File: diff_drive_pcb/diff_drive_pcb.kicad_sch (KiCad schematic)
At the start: 13 parts, among them J1 Conn_01x02_Pin, J10 Conn_01x02_Pin, J2 Conn_01x04_Socket, J3 Conn_01x02_Pin, J4 Conn_01x04_Socket, J5 Conn_01x02_Pin, J6 Conn_01x04_Socket, J7 Conn_01x02_Pin, J8 Conn_01x04_Socket, J9 Conn_01x02_Pin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

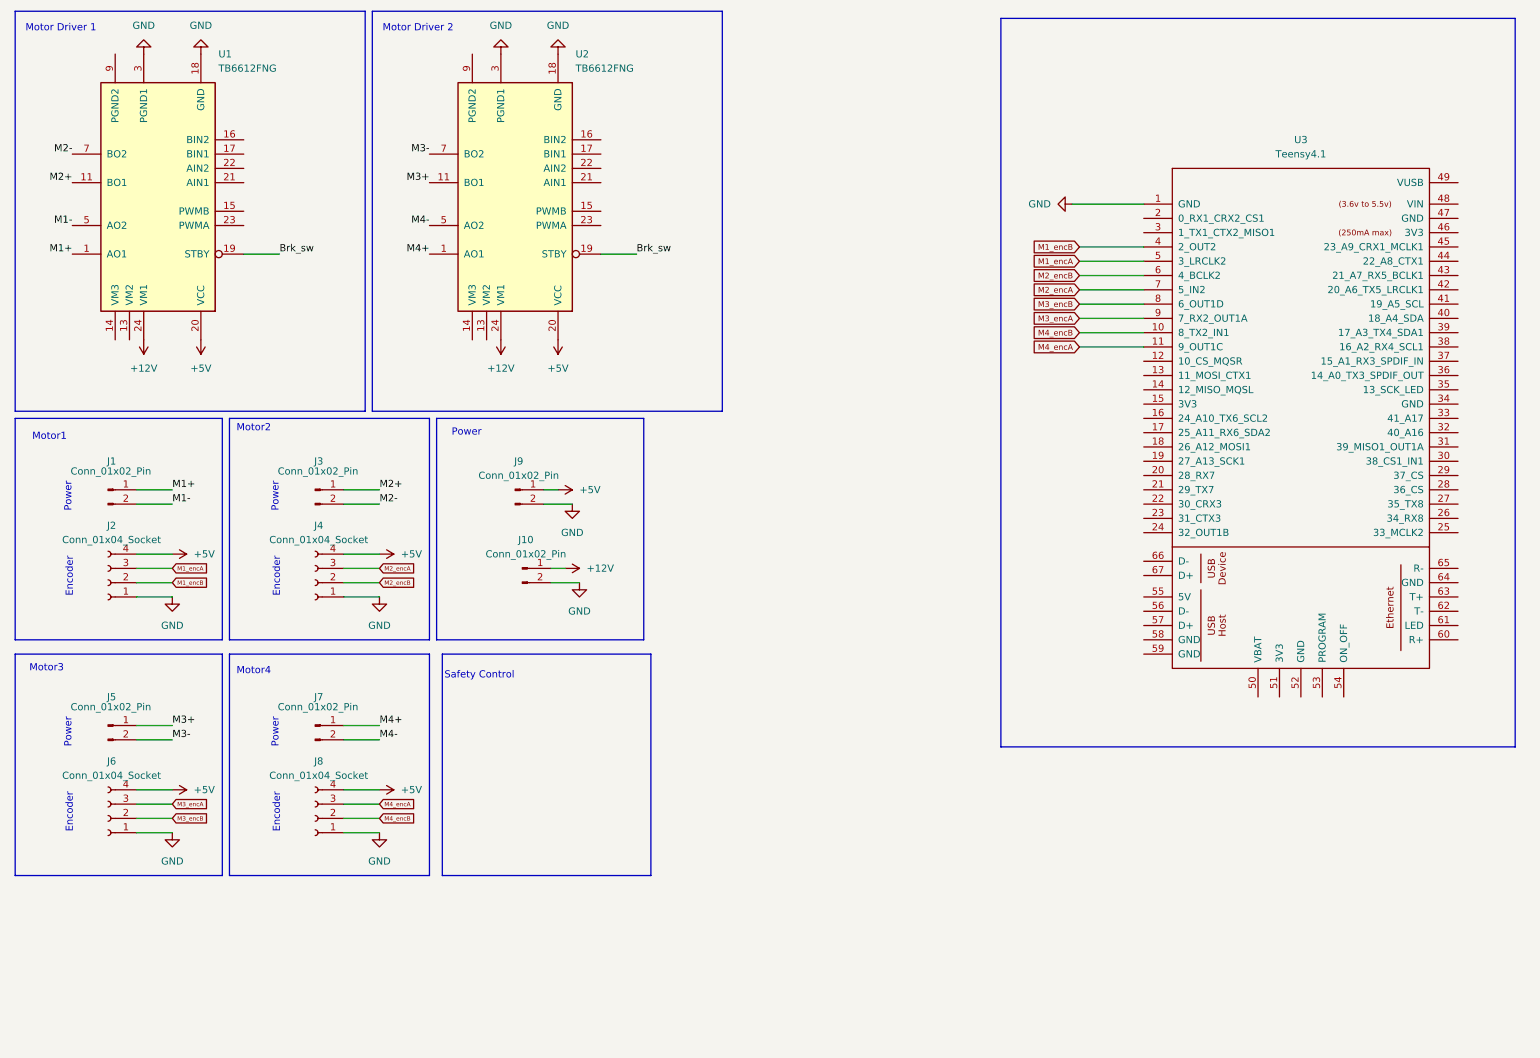
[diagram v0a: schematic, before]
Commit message: Added sensors and command signals to schematic
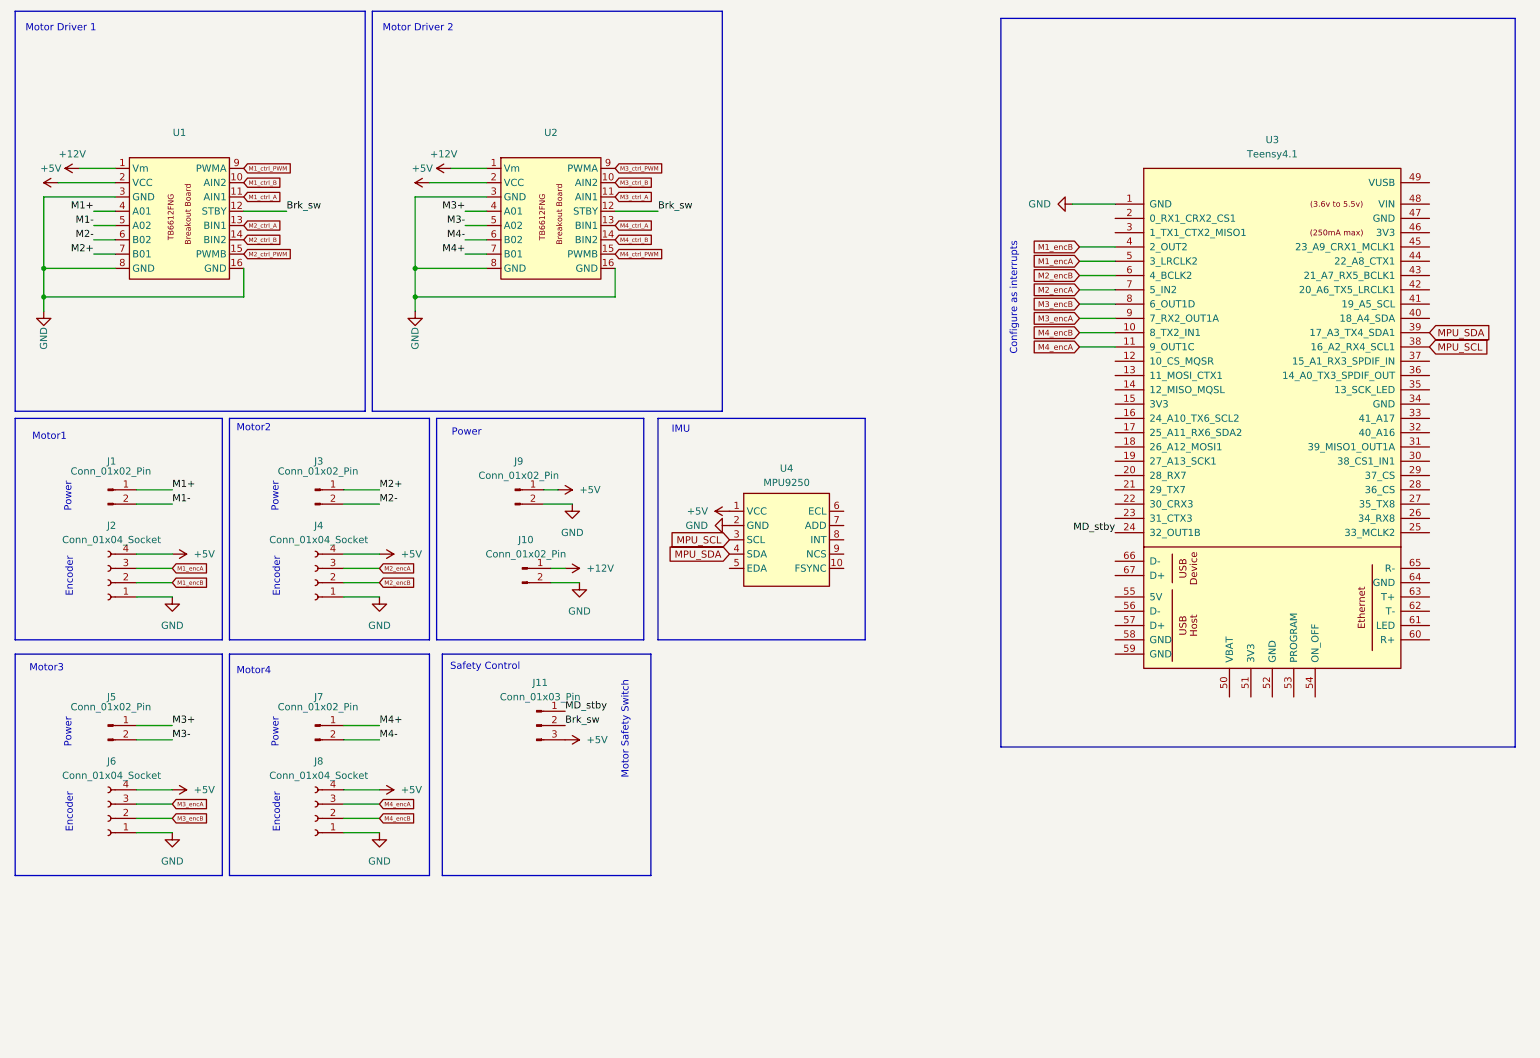
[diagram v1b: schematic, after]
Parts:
- removed U1, U2: TB6612FNG, Package_SO:SSOP-24_5.3x8.2mm_P0.65mm, symbol Driver_Motor:TB6612FNG
- added J11: Conn_01x03_Pin, Connector_PinHeader_2.54mm:PinHeader_1x03_P2.54mm_Vertical, symbol Connector:Conn_01x03_Pin
- added U1, U2: ~, symbol TB6612FNG:TB6612FNG
- added U4: MPU9250, Connector_PinHeader_2.54mm:PinHeader_1x08_P2.54mm_Vertical, symbol mpu9250:MPU9250
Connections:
- net +12V: now also U1.1 (Vm), U2.1 (Vm)
- net +5V: now also J11.3 (Pin_3), U1.2 (VCC), U2.2 (VCC), U4.1 (VCC)
- net Brk_sw: now also J11.2 (Pin_2), U1.12 (STBY), U2.12 (STBY)
- net GND: now also U1.16 (GND), U1.3 (GND), U1.8 (GND), U2.16 (GND), U2.3 (GND), U2.8 (GND), U4.2 (GND)
- net M1+: now also U1.4 (A01)
- net M1-: now also U1.5 (A02)
- net M2+: now also U1.7 (B01)
- net M2-: now also U1.6 (B02)
- net M3+: now also U2.4 (A01)
- net M3-: now also U2.5 (A02)
- net M4+: now also U2.7 (B01)
- net M4-: now also U2.6 (B02)
- net MD_stby: now reaches U3.24 (32_OUT1B)
- net MD_stby: now also J11.1 (Pin_1)
- net MPU_SCL: now reaches U3.38 (16_A2_RX4_SCL1)
- net MPU_SCL: now also U4.3 (SCL)
- net MPU_SDA: now reaches U3.39 (17_A3_TX4_SDA1)
- net MPU_SDA: now also U4.4 (SDA)
- new net M1_ctrl_A: U1.11 (AIN1)
- new net M1_ctrl_B: U1.10 (AIN2)
- new net M1_ctrl_PWM: U1.9 (PWMA)
- new net M2_ctrl_A: U1.13 (BIN1)
- new net M2_ctrl_B: U1.14 (BIN2)
- new net M2_ctrl_PWM: U1.15 (PWMB)
- new net M3_ctrl_A: U2.11 (AIN1)
- new net M3_ctrl_B: U2.10 (AIN2)
- new net M3_ctrl_PWM: U2.9 (PWMA)
- new net M4_ctrl_A: U2.13 (BIN1)
- new net M4_ctrl_B: U2.14 (BIN2)
- new net M4_ctrl_PWM: U2.15 (PWMB)
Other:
- note added: "Configure as interrupts"
- note added: "IMU"
- note added: "Motor Safety Switch"

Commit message: PCB v1.0 developed
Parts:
- removed U4: MPU9250, Connector_PinHeader_2.54mm:PinHeader_1x08_P2.54mm_Vertical, symbol mpu9250:MPU9250
- added BZ1, BZ3: Buzzer, Buzzer_Beeper:Buzzer_TDK_PS1240P02BT_D12.2mm_H6.5mm, symbol Device:Buzzer
- J1: value Conn_01x02_Pin -> P_M1
- J10: value Conn_01x02_Pin -> 12V_IN
- J11: value Conn_01x03_Pin -> Motor_Break_SW
- J2: value Conn_01x04_Socket -> Encoder_M1
- J3: value Conn_01x02_Pin -> P_M2
- J4: value Conn_01x04_Socket -> Encoder_M2
- J5: value Conn_01x02_Pin -> P_M3
- J6: value Conn_01x04_Socket -> Encoder_M3
- J7: value Conn_01x02_Pin -> P_M4
- J8: value Conn_01x04_Socket -> Encoder_M4
- J9: value Conn_01x02_Pin -> 5V_IN
- U1: value ~ -> Motor Driver1; footprint (none) -> TB6612FNG:TB6612FNG breakout board
- U2: value ~ -> Motor Driver 2; footprint (none) -> TB6612FNG:TB6612FNG breakout board
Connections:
- net GND: now also BZ1.2 (-), BZ3.2 (-)
- net M1_ctrl_A: now also U3.6 (4_BCLK2)
- net M1_ctrl_B: now also U3.5 (3_LRCLK2)
- net M1_ctrl_PWM: now also U3.4 (2_OUT2)
- net M1_encA: now also U3.31 (39_MISO1_OUT1A); no longer U3.5 (3_LRCLK2)
- net M1_encB: now also U3.32 (40_A16); no longer U3.4 (2_OUT2)
- net M2_ctrl_A: now also U3.7 (5_IN2)
- net M2_ctrl_B: now also U3.8 (6_OUT1D)
- net M2_ctrl_PWM: now also U3.9 (7_RX2_OUT1A)
- net M2_encA: now also U3.29 (37_CS); no longer U3.7 (5_IN2)
- net M2_encB: now also U3.30 (38_CS1_IN1); no longer U3.6 (4_BCLK2)
- net M3_ctrl_A: now also U3.12 (10_CS_MQSR)
- net M3_ctrl_B: now also U3.11 (9_OUT1C)
- net M3_ctrl_PWM: now also U3.10 (8_TX2_IN1)
- net M3_encA: now also U3.27 (35_TX8); no longer U3.9 (7_RX2_OUT1A)
- net M3_encB: now also U3.28 (36_CS); no longer U3.8 (6_OUT1D)
- net M4_ctrl_A: now also U3.13 (11_MOSI_CTX1)
- net M4_ctrl_B: now also U3.14 (12_MISO_MQSL)
- net M4_ctrl_PWM: now also U3.16 (24_A10_TX6_SCL2)
- net M4_encA: now also U3.25 (33_MCLK2); no longer U3.11 (9_OUT1C)
- net M4_encB: now also U3.26 (34_RX8); no longer U3.10 (8_TX2_IN1)
- net HEADLIGHTS: now reaches U3.19 (27_A13_SCK1)
- net XSHUT1: now reaches U3.20 (28_RX7)
- net XSHUT2: now reaches U3.21 (29_TX7)
- net XSHUT3: now reaches U3.22 (30_CRX3)
- net XSHUT4: now reaches U3.23 (31_CTX3)
- net STATUS_LED3: now reaches U3.42 (20_A6_TX5_LRCLK1)
- net STATUS_LED2: now reaches U3.43 (21_A7_RX5_BCLK1)
- net STATUS_LED1: now reaches U3.44 (22_A8_CTX1)
- net Buzzer_ctl: now reaches U3.45 (23_A9_CRX1_MCLK1)
- net Buzzer_ctl: now also BZ1.1 (+), BZ3.1 (+)
- net +3V3: now reaches U3.46 (3V3)
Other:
- added sheet Sensor_con (tof.kicad_sch)
- added sheet power_outputs (p_out.kicad_sch)
- note added: "Debug System"
- note removed: "IMU"
- moved on the sheet: U3

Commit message: Updated Schematic
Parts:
- removed U1: Motor Driver1, TB6612FNG:TB6612FNG breakout board, symbol TB6612FNG:TB6612FNG
- removed U2: Motor Driver 2, TB6612FNG:TB6612FNG breakout board, symbol TB6612FNG:TB6612FNG
- added U1: Motor Driver 1, MDD3A:MDD3A, symbol MDD3A:MDD3A
- added U2: Motor Driver 2, MDD3A:MDD3A, symbol MDD3A:MDD3A
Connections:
- net +12V: now also U1.11 (+12V), U2.11 (+12V)
- net +5V: now also U3.48 (VIN); no longer J11.3 (Pin_3)
- net Brk_sw: now also U1.4 (GND), U2.4 (GND)
- net GND: now also J11.3 (Pin_3)
- net M1+: now also U1.7 (M1+)
- net M1-: now also U1.8 (M1-)
- net M1_ctrl_A: now also U3.5 (3_LRCLK2), U1.1 (M1A); no longer U3.6 (4_BCLK2)
- net M1_ctrl_B: now also U3.6 (4_BCLK2), U1.2 (M1B); no longer U3.5 (3_LRCLK2)
- net M1_encA: now also U3.20 (28_RX7); no longer U3.31 (39_MISO1_OUT1A)
- net M1_encB: now also U3.21 (29_TX7); no longer U3.32 (40_A16)
- net M2+: now also U1.9 (M2+)
- net M2-: now also U1.10 (M2-)
- net M2_ctrl_A: now also U1.5 (M2A)
- net M2_ctrl_B: now also U1.6 (M2B)
- net M2_encA: now also U3.22 (30_CRX3); no longer U3.29 (37_CS)
- net M2_encB: now also U3.23 (31_CTX3); no longer U3.30 (38_CS1_IN1)
- net M3+: now also U2.7 (M1+)
- net M3-: now also U2.8 (M1-)
- net M3_ctrl_A: now also U3.11 (9_OUT1C), U2.1 (M1A); no longer U3.12 (10_CS_MQSR)
- net M3_ctrl_B: now also U3.12 (10_CS_MQSR), U2.2 (M1B); no longer U3.11 (9_OUT1C)
- net M4+: now also U2.9 (M2+)
- net M4-: now also U2.10 (M2-)
- net M4_ctrl_A: now also U2.5 (M2A)
- net M4_ctrl_B: now also U2.6 (M2B)
- net XSHUT1: now also U3.32 (40_A16); no longer U3.20 (28_RX7)
- net XSHUT2: now also U3.31 (39_MISO1_OUT1A); no longer U3.21 (29_TX7)
- net XSHUT3: now also U3.30 (38_CS1_IN1); no longer U3.22 (30_CRX3)
- net XSHUT4: now also U3.29 (37_CS); no longer U3.23 (31_CTX3)
- net M1_ctrl_PWM: no longer names the net of U3.4 (2_OUT2)
- net M2_ctrl_PWM: no longer names the net of U3.9 (7_RX2_OUT1A)
- net M3_ctrl_PWM: no longer names the net of U3.10 (8_TX2_IN1)
- net M4_ctrl_PWM: no longer names the net of U3.16 (24_A10_TX6_SCL2)
- no-connect marks 0 -> 38
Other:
- removed sheet power_outputs
- moved on the sheet: U3

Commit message: Rev 2.1 pcb design
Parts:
- added J12: POWER_SW, Connector_JST:JST_XH_B2B-XH-AM_1x02_P2.50mm_Vertical, symbol Connector:Conn_01x02_Pin
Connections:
- net +5V: now also J12.1 (Pin_1); no longer J9.1 (Pin_1)
- net Buzzer_ctl: now also U3.23 (31_CTX3); no longer U3.45 (23_A9_CRX1_MCLK1)
- net HEADLIGHTS: now also U3.44 (22_A8_CTX1); no longer U3.19 (27_A13_SCK1)
- net M1_encA: now also U3.31 (39_MISO1_OUT1A); no longer U3.20 (28_RX7)
- net M1_encB: now also U3.32 (40_A16); no longer U3.21 (29_TX7)
- net M2_encA: now also U3.29 (37_CS); no longer U3.22 (30_CRX3)
- net M2_encB: now also U3.30 (38_CS1_IN1); no longer U3.23 (31_CTX3)
- net MD_stby: now also U3.10 (8_TX2_IN1); no longer U3.24 (32_OUT1B)
- net STATUS_LED1: now also U3.43 (21_A7_RX5_BCLK1); no longer U3.44 (22_A8_CTX1)
- net STATUS_LED2: now also U3.42 (20_A6_TX5_LRCLK1); no longer U3.43 (21_A7_RX5_BCLK1)
- net STATUS_LED3: now also U3.41 (19_A5_SCL); no longer U3.42 (20_A6_TX5_LRCLK1)
- net XSHUT1: now also U3.19 (27_A13_SCK1); no longer U3.32 (40_A16)
- net XSHUT2: now also U3.20 (28_RX7); no longer U3.31 (39_MISO1_OUT1A)
- net XSHUT3: now also U3.21 (29_TX7); no longer U3.30 (38_CS1_IN1)
- net XSHUT4: now also U3.22 (30_CRX3); no longer U3.29 (37_CS)
- new net mc_power: J12.2 (Pin_2), J9.1 (Pin_1)

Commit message: Cleaned up PCB and adjusted size
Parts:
- J1, J10, J12, J3, J5, J7, J9: footprint Connector_JST:JST_XH_B2B-XH-AM_1x02_P2.50mm_Vertical -> Connector_JST:JST_XH_B2B-XH-A_1x02_P2.50mm_Vertical
- J2, J4, J6, J8: footprint Connector_JST:JST_XH_B4B-XH-AM_1x04_P2.50mm_Vertical -> Connector_JST:JST_XH_B4B-XH-A_1x04_P2.50mm_Vertical
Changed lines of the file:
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@@
 			)
 		)
-		(property "Footprint" "Connector_JST:JST_XH_B2B-XH-AM_1x02_P2.50mm_Vertical"
+		(property "Footprint" "Connector_JST:JST_XH_B2B-XH-A_1x02_P2.50mm_Vertical"
 			(at 105.41 111.76 0)
 			(effects
@@
 			)
 		)
-		(property "Footprint" "Connector_JST:JST_XH_B4B-XH-AM_1x04_P2.50mm_Vertical"
+		(property "Footprint" "Connector_JST:JST_XH_B4B-XH-A_1x04_P2.50mm_Vertical"
 			(at 68.58 156.21 0)
 			(effects
@@
 			)
 		)
-		(property "Footprint" "Connector_JST:JST_XH_B2B-XH-AM_1x02_P2.50mm_Vertical"
+		(property "Footprint" "Connector_JST:JST_XH_B2B-XH-A_1x02_P2.50mm_Vertical"
 			(at 102.87 154.94 0)
 			(effects
@@
 			)
 		)
-		(property "Footprint" "Connector_JST:JST_XH_B2B-XH-AM_1x02_P2.50mm_Vertical"
+		(property "Footprint" "Connector_JST:JST_XH_B2B-XH-A_1x02_P2.50mm_Vertical"
 			(at 68.58 139.7 0)
 			(effects
@@
 			)
 		)
-		(property "Footprint" "Connector_JST:JST_XH_B4B-XH-AM_1x04_P2.50mm_Vertical"
+		(property "Footprint" "Connector_JST:JST_XH_B4B-XH-A_1x04_P2.50mm_Vertical"
 			(at 31.75 114.3 0)
 			(effects
@@
 			)
 		)
-		(property "Footprint" "Connector_JST:JST_XH_B4B-XH-AM_1x04_P2.50mm_Vertical"
+		(property "Footprint" "Connector_JST:JST_XH_B4B-XH-A_1x04_P2.50mm_Vertical"
 			(at 31.75 156.21 0)
 			(effects
@@
 			)
 		)
-		(property "Footprint" "Connector_JST:JST_XH_B2B-XH-AM_1x02_P2.50mm_Vertical"
+		(property "Footprint" "Connector_JST:JST_XH_B2B-XH-A_1x02_P2.50mm_Vertical"
 			(at 31.75 97.79 0)
 			(effects
@@
 			)
 		)
-		(property "Footprint" "Connector_JST:JST_XH_B2B-XH-AM_1x02_P2.50mm_Vertical"
+		(property "Footprint" "Connector_JST:JST_XH_B2B-XH-A_1x02_P2.50mm_Vertical"
 			(at 104.14 97.79 0)
 			(effects
@@
 			)
 		)
-		(property "Footprint" "Connector_JST:JST_XH_B2B-XH-AM_1x02_P2.50mm_Vertical"
+		(property "Footprint" "Connector_JST:JST_XH_B2B-XH-A_1x02_P2.50mm_Vertical"
 			(at 68.58 97.79 0)
 			(effects
@@
 			)
 		)
-		(property "Footprint" "Connector_JST:JST_XH_B4B-XH-AM_1x04_P2.50mm_Vertical"
+		(property "Footprint" "Connector_JST:JST_XH_B4B-XH-A_1x04_P2.50mm_Vertical"
 			(at 68.58 114.3 0)
 			(effects
@@
 			)
 		)
-		(property "Footprint" "Connector_JST:JST_XH_B2B-XH-AM_1x02_P2.50mm_Vertical"
+		(property "Footprint" "Connector_JST:JST_XH_B2B-XH-A_1x02_P2.50mm_Vertical"
 			(at 31.75 139.7 0)
 			(effects
